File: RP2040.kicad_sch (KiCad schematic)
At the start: 17 parts, among them U1 RP2040, Y1 12M

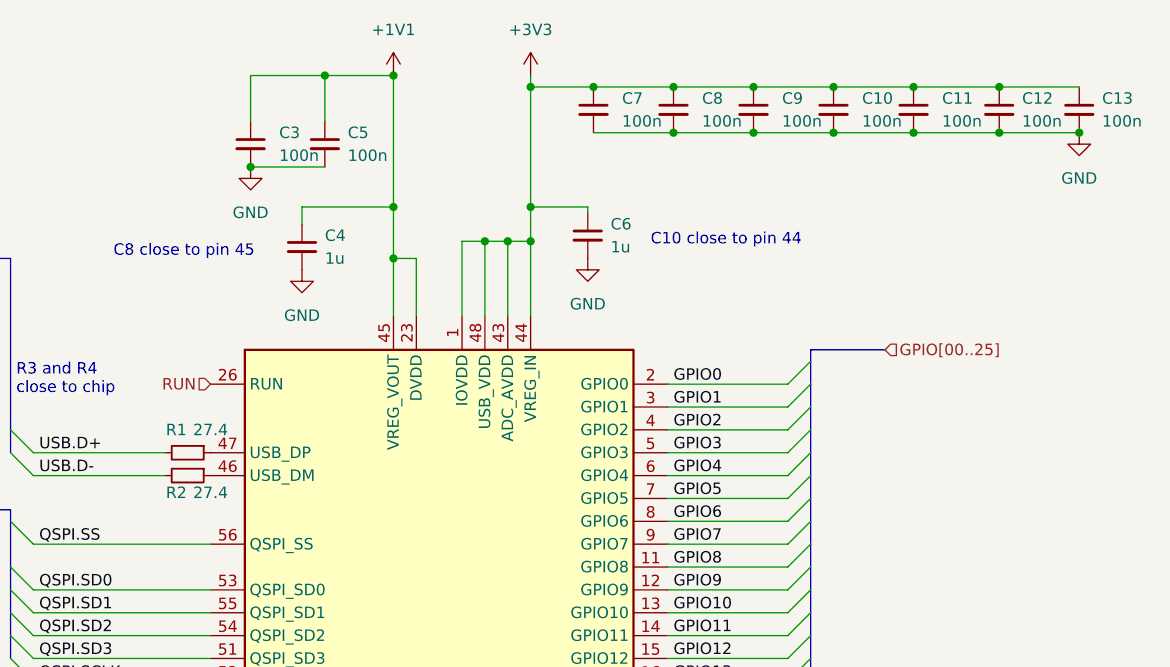
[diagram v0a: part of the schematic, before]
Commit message: Fixed duplicate annotations
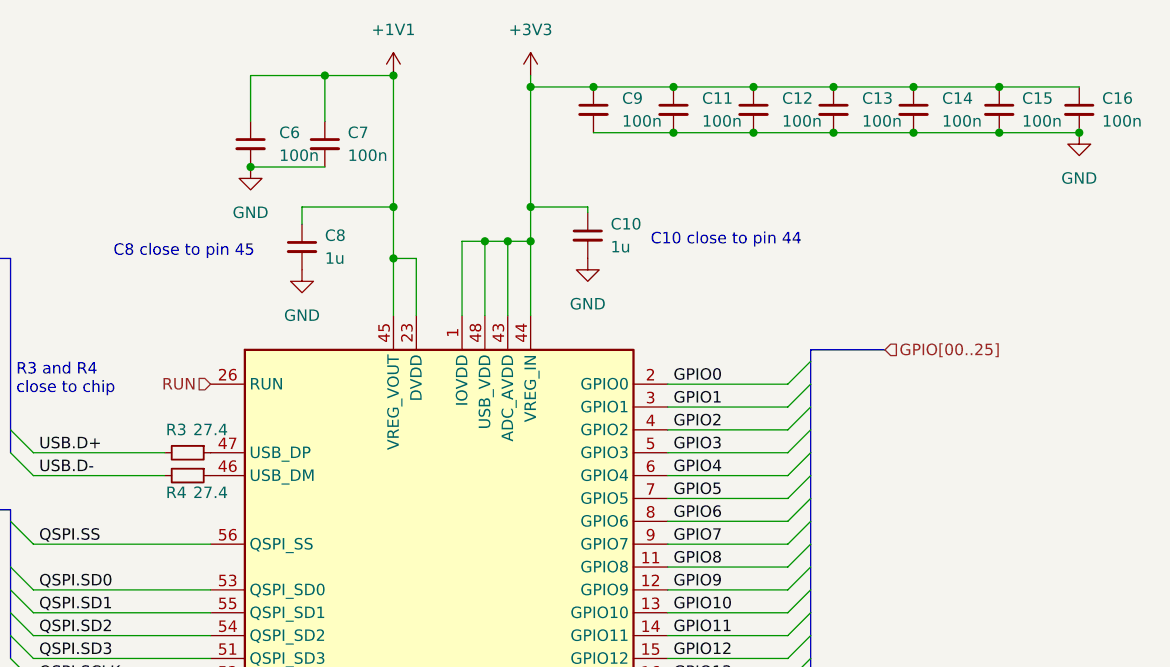
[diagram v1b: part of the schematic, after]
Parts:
- renumbered C6 to C10, C8 to C11, C9 to C12, C10 to C13, C11 to C14, C12 to C15, C13 to C16, C3 to C6, C5 to C7, C4 to C8, C7 to C9, R1 to R3, R2 to R4
